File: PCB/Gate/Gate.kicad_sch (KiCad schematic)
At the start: 140 parts, among them J1 USB-C, J2 Shelly, P1 TestPoint, P10 TestPoint, P11 TestPoint, P12 TestPoint, P13 TestPoint, P2 TestPoint, P3 TestPoint, P4 TestPoint, P5 TestPoint, P6 TestPoint, P7 TestPoint, P8 TestPoint, P9 TestPoint, T1 TestPoint, T10 TestPoint, T11 TestPoint, T12 TestPoint, T13 TestPoint, T2 TestPoint, T3 TestPoint, T4 TestPoint, T5 TestPoint, T6 TestPoint, T7 TestPoint, T8 TestPoint, T9 TestPoint, U1 ESP32-PICO-MINI-02, U2 LMR16006XDDCR, U3 QR

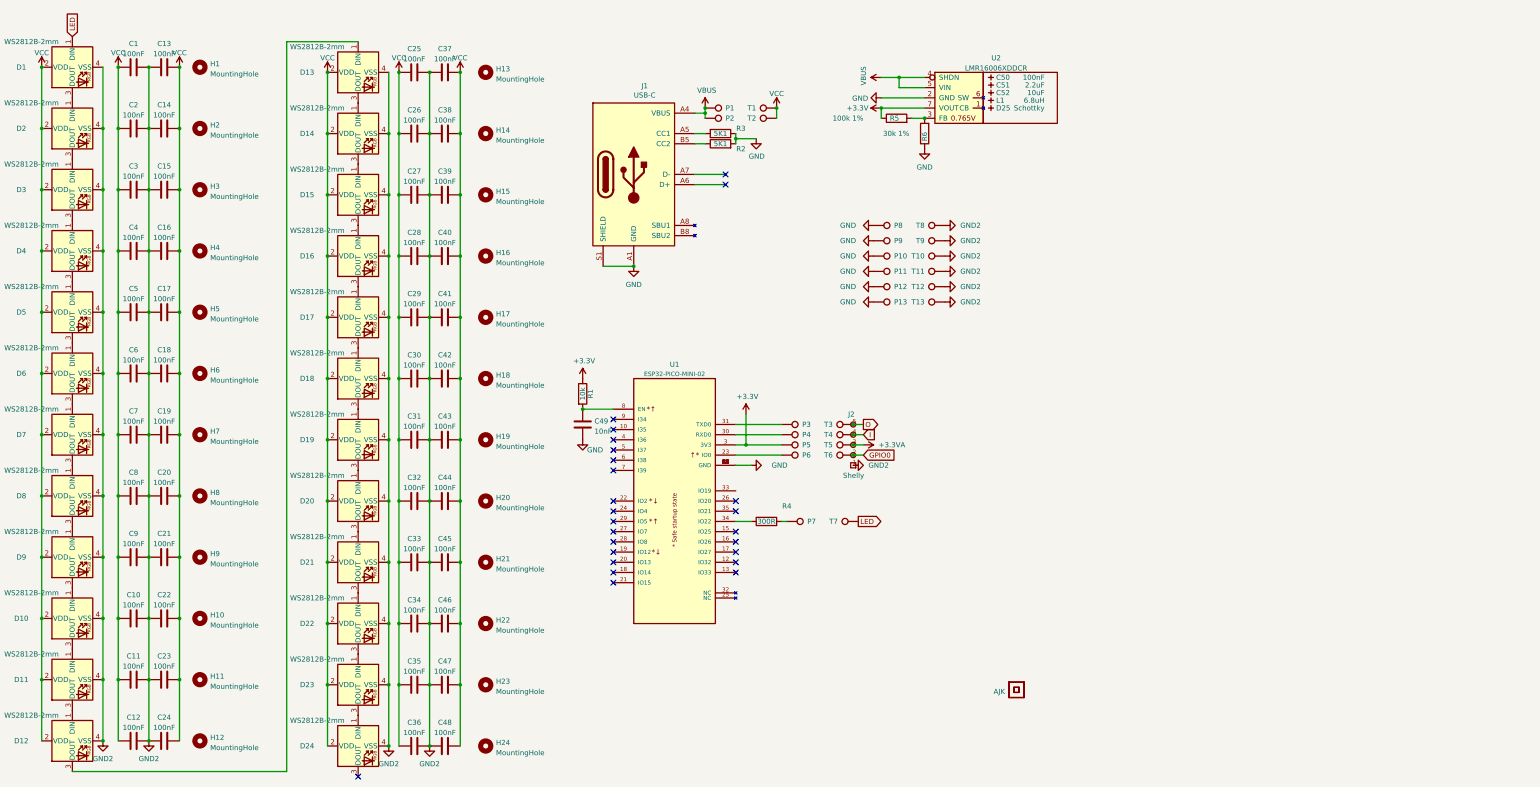
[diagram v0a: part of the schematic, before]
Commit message: Changed pads for easier soldering next time
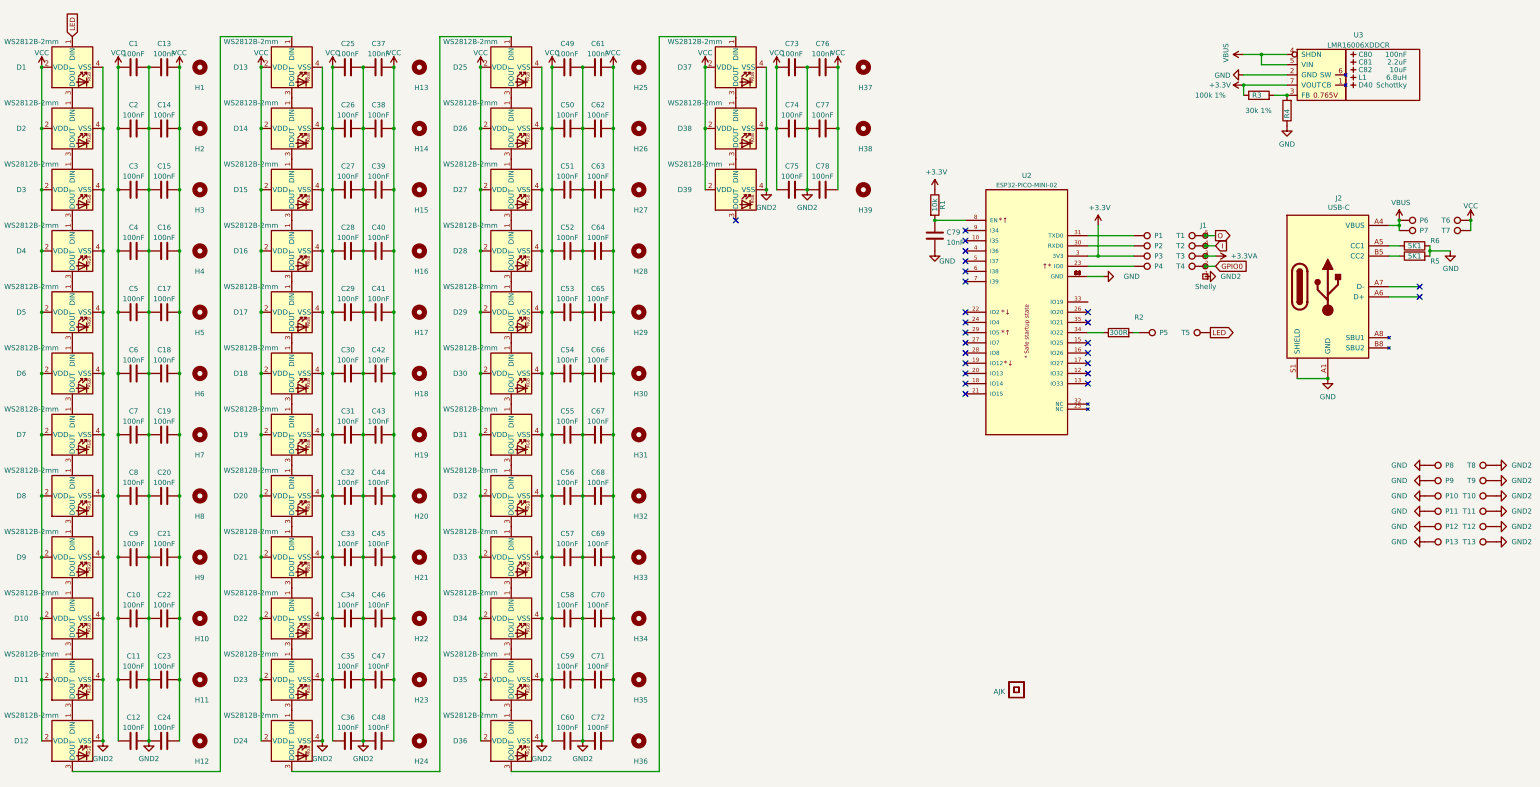
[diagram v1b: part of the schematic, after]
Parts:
- added C49, C50, C51, C52, C53, C54, C55, C56, C57, C58, C59, C60, C61, C62, C63, C64, C65, C66, C67, C68, C69, C70, C71, C72, C73, C74, C75, C76, C77, C78: 100nF, RevK:C_0603, symbol Device:C
- added D25, D26, D27, D28, D29, D30, D31, D32, D33, D34, D35, D36, D37, D38, D39: WS2812B-2mm, RevK:SMD2020, symbol RevK:WS2812B-2mm
- added H25, H26, H27, H28, H29, H30, H31, H32, H33, H34, H35, H36, H37, H38, H39: MountingHole, RevK:LEDHOLE, symbol Mechanical:MountingHole
- renumbered C49 to C79, C50 to C80, C51 to C81, C52 to C82, D25 to D40, J2 to J1, J1 to J2, P3 to P1, P4 to P2, P5 to P3, P6 to P4, P7 to P5, P1 to P6, P2 to P7, R4 to R2, R5 to R3, R6 to R4, R2 to R5, R3 to R6, T3 to T1, T4 to T2, T5 to T3, T6 to T4, T7 to T5, T1 to T6, T2 to T7, U3 to U1, U1 to U2, U2 to U3
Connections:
- net GND2: now also C49.2, C50.2, C51.2, C52.2, C53.2, C54.2, C55.2, C56.2, C57.2, C58.2, C59.2, C60.2, C61.2, C62.2, C63.2, C64.2, C65.2, C66.2, C67.2, C68.2, C69.2, C70.2, C71.2, C72.2, C73.2, C74.2, C75.2, C76.2, C77.2, C78.2, D25.4 (VSS), D26.4 (VSS), D27.4 (VSS), D28.4 (VSS), D29.4 (VSS), D30.4 (VSS), D31.4 (VSS), D32.4 (VSS), D33.4 (VSS), D34.4 (VSS), D35.4 (VSS), D36.4 (VSS), D37.4 (VSS), D38.4 (VSS), D39.4 (VSS)
- net VCC: now also C49.1, C50.1, C51.1, C52.1, C53.1, C54.1, C55.1, C56.1, C57.1, C58.1, C59.1, C60.1, C61.1, C62.1, C63.1, C64.1, C65.1, C66.1, C67.1, C68.1, C69.1, C70.1, C71.1, C72.1, C73.1, C74.1, C75.1, C76.1, C77.1, C78.1, D25.2 (VDD), D26.2 (VDD), D27.2 (VDD), D28.2 (VDD), D29.2 (VDD), D30.2 (VDD), D31.2 (VDD), D32.2 (VDD), D33.2 (VDD), D34.2 (VDD), D35.2 (VDD), D36.2 (VDD), D37.2 (VDD), D38.2 (VDD), D39.2 (VDD)
- net at D24.3 (DOUT): now also D25.1 (DIN)
- new net: D37.3 (DOUT), D38.1 (DIN)
- new net: D38.3 (DOUT), D39.1 (DIN)
- new net: D26.3 (DOUT), D27.1 (DIN)
- new net: D27.3 (DOUT), D28.1 (DIN)
- new net: D29.3 (DOUT), D30.1 (DIN)
- new net: D30.3 (DOUT), D31.1 (DIN)
- new net: D28.3 (DOUT), D29.1 (DIN)
- new net: D33.3 (DOUT), D34.1 (DIN)
- new net: D34.3 (DOUT), D35.1 (DIN)
- new net: D32.3 (DOUT), D33.1 (DIN)
- new net: D25.3 (DOUT), D26.1 (DIN)
- new net: D35.3 (DOUT), D36.1 (DIN)
- new net: D36.3 (DOUT), D37.1 (DIN)
- new net: D31.3 (DOUT), D32.1 (DIN)
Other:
- moved on the sheet: C25, C26, C27, C28, C29, C30, C31, C32, C33, C34, C35, C36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

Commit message: Start on ring
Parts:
- removed C80: 100nF, RevK:C_0603_, symbol RevK:Hidden
- removed C81: 2.2uF, RevK:C_0805_, symbol RevK:Hidden
- removed C82: 10uF, RevK:C_0805_, symbol RevK:Hidden
- removed D1, D10, D11, D12, D13, D14, D15, D16, D17, D18, D19, D2, D20, D21, D22, D23, D24, D25, D26, D27, D28, D29, D3, D30, D31, D32, D33, D34, D35, D36, D37, D38, D39, D4, D5, D6, D7, D8, D9: WS2812B-2mm, RevK:SMD2020, symbol RevK:WS2812B-2mm
- removed D40: Schottky, RevK:D_1206_, symbol RevK:Hidden
- removed H1, H10, H11, H12, H13, H14, H15, H16, H17, H18, H19, H2, H20, H21, H22, H23, H24, H25, H26, H27, H28, H29, H3, H30, H31, H32, H33, H34, H35, H36, H37, H38, H39, H4, H5, H6, H7, H8, H9: MountingHole, RevK:LEDHOLE, symbol Mechanical:MountingHole
- removed J1: Shelly, RevK:Shelly, symbol RevK:Shelly
- removed J2: USB-C, RevK:USC16-TR, symbol RevK:USB-C
- removed L1: 6.8uH, RevK:L_4x4_, symbol RevK:Hidden
- removed P1, P10, P11, P12, P13, P2, P3, P4, P5, P6, P7, P8, P9: TestPoint, RevK:PAD, symbol Connector:TestPoint
- removed R1: 10k, RevK:R_0603, symbol Device:R
- removed R2: 300R, RevK:R_0603, symbol Device:R
- removed R3: 100k 1%, RevK:R_0603, symbol Device:R
- removed R4: 30k 1%, RevK:R_0603, symbol Device:R
- removed R5, R6: 5K1, RevK:R_0603, symbol Device:R
- removed T1, T10, T11, T12, T13, T2, T3, T4, T5, T6, T7, T8, T9: TestPoint, RevK:PAD-LINK, symbol Connector:TestPoint
- removed U2: ESP32-PICO-MINI-02, RevK:ESP32-PICO-MINI-02, symbol RevK:ESP32-PICO-MINI-02
- removed U3: LMR16006XDDCR, RevK:SOT-23-Thin-6-Reg, symbol RevK:LMR16006XDDCR
- added C100, C101, C102, C103, C104, C105, C106, C107, C108, C109, C110, C111, C112, C113, C114, C115, C116, C117, C80, C81, C82, C83, C84, C85, C86, C87, C88, C89, C90, C91, C92, C93, C94, C95, C96, C97, C98, C99: 330nF, RevK:C_0402, symbol Device:C
- added D1, D10, D100, D101, D102, D103, D104, D105, D106, D107, D108, D109, D11, D110, D111, D112, D113, D114, D115, D116, D117, D12, D13, D14, D15, D16, D17, D18, D19, D2, D20, D21, D22, D23, D24, D25, D26, D27, D28, D29, D3, D30, D31, D32, D33, D34, D35, D36, D37, D38, D39, D4, D40, D41, D42, D43, D44, D45, D46, D47, D48, D49, D5, D50, D51, D52, D53, D54, D55, D56, D57, D58, D59, D6, D60, D61, D62, D63, D64, D65, D66, D67, D68, D69, D7, D70, D71, D72, D73, D74, D75, D76, D77, D78, D79, D8, D80, D81, D82, D83, D84, D85, D86, D87, D88, D89, D9, D90, D91, D92, D93, D94, D95, D96, D97, D98, D99: XL-1010RGBC-WS2812B, RevK:SMD1010, symbol RevK:WS2812B-1mm
- C1, C10, C11, C12, C13, C14, C15, C16, C17, C18, C19, C2, C20, C21, C22, C23, C24, C25, C26, C27, C28, C29, C3, C30, C31, C32, C33, C34, C35, C36, C37, C38, C39, C4, C40, C41, C42, C43, C44, C45, C46, C47, C48, C49, C5, C50, C51, C52, C53, C54, C55, C56, C57, C58, C59, C6, C60, C61, C62, C63, C64, C65, C66, C67, C68, C69, C7, C70, C71, C72, C73, C74, C75, C76, C77, C78, C8, C9: value 100nF -> 330nF; footprint RevK:C_0603 -> RevK:C_0402
- C79: value 10nF -> 330nF; footprint Capacitor_SMD:C_0603_1608Metric -> RevK:C_0402
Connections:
- net GND2 is gone; now on net GND: C1.2, C10.2, C11.2, C12.2, C13.2, C14.2, C15.2, C16.2, C17.2, C18.2, C19.2, C2.2, C20.2, C21.2, C22.2, C23.2, C24.2, C25.2, C26.2, C27.2, C28.2, C29.2, C3.2, C30.2, C31.2, C32.2, C33.2, C34.2, C35.2, C36.2, C37.2, C38.2, C39.2, C4.2, C40.2, C41.2, C42.2, C43.2, C44.2, C45.2, C46.2, C47.2, C48.2, C49.2, C5.2, C50.2, C51.2, C52.2, C53.2, C54.2, C55.2, C56.2, C57.2, C58.2, C59.2, C6.2, C60.2, C61.2, C62.2, C63.2, C64.2, C65.2, C66.2, C67.2, C68.2, C69.2, C7.2, C70.2, C71.2, C72.2, C73.2, C74.2, C75.2, C76.2, C77.2, C78.2, C8.2, C9.2
- net GND: now also C79.2, C100.2, C101.2, C102.2, C103.2, C104.2, C105.2, C106.2, C107.2, C108.2, C109.2, C110.2, C111.2, C112.2, C113.2, C114.2, C115.2, C116.2, C117.2, C80.2, C81.2, C82.2, C83.2, C84.2, C85.2, C86.2, C87.2, C88.2, C89.2, C90.2, C91.2, C92.2, C93.2, C94.2, C95.2, C96.2, C97.2, C98.2, C99.2, D1.3 (-), D10.3 (-), D100.3 (-), D101.3 (-), D102.3 (-), D103.3 (-), D104.3 (-), D105.3 (-), D106.3 (-), D107.3 (-), D108.3 (-), D109.3 (-), D11.3 (-), D110.3 (-), D111.3 (-), D112.3 (-), D113.3 (-), D114.3 (-), D115.3 (-), D116.3 (-), D117.3 (-), D12.3 (-), D13.3 (-), D14.3 (-), D15.3 (-), D16.3 (-), D17.3 (-), D18.3 (-), D19.3 (-), D2.3 (-), D20.3 (-), D21.3 (-), D22.3 (-), D23.3 (-), D24.3 (-), D25.3 (-), D26.3 (-), D27.3 (-), D28.3 (-), D29.3 (-), D3.3 (-), D30.3 (-), D31.3 (-), D32.3 (-), D33.3 (-), D34.3 (-), D35.3 (-), D36.3 (-), D37.3 (-), D38.3 (-), D39.3 (-), D4.3 (-), D40.3 (-), D41.3 (-), D42.3 (-), D43.3 (-), D44.3 (-), D45.3 (-), D46.3 (-), D47.3 (-), D48.3 (-), D49.3 (-), D5.3 (-), D50.3 (-), D51.3 (-), D52.3 (-), D53.3 (-), D54.3 (-), D55.3 (-), D56.3 (-), D57.3 (-), D58.3 (-), D59.3 (-), D6.3 (-), D60.3 (-), D61.3 (-), D62.3 (-), D63.3 (-), D64.3 (-), D65.3 (-), D66.3 (-), D67.3 (-), D68.3 (-), D69.3 (-), D7.3 (-), D70.3 (-), D71.3 (-), D72.3 (-), D73.3 (-), D74.3 (-), D75.3 (-), D76.3 (-), D77.3 (-), D78.3 (-), D79.3 (-), D8.3 (-), D80.3 (-), D81.3 (-), D82.3 (-), D83.3 (-), D84.3 (-), D85.3 (-), D86.3 (-), D87.3 (-), D88.3 (-), D89.3 (-), D9.3 (-), D90.3 (-), D91.3 (-), D92.3 (-), D93.3 (-), D94.3 (-), D95.3 (-), D96.3 (-), D97.3 (-), D98.3 (-), D99.3 (-); no longer C79.1
- net VCC: now also C79.1, C100.1, C101.1, C102.1, C103.1, C104.1, C105.1, C106.1, C107.1, C108.1, C109.1, C110.1, C111.1, C112.1, C113.1, C114.1, C115.1, C116.1, C117.1, C80.1, C81.1, C82.1, C83.1, C84.1, C85.1, C86.1, C87.1, C88.1, C89.1, C90.1, C91.1, C92.1, C93.1, C94.1, C95.1, C96.1, C97.1, C98.1, C99.1, D1.2 (+), D10.2 (+), D100.2 (+), D101.2 (+), D102.2 (+), D103.2 (+), D104.2 (+), D105.2 (+), D106.2 (+), D107.2 (+), D108.2 (+), D109.2 (+), D11.2 (+), D110.2 (+), D111.2 (+), D112.2 (+), D113.2 (+), D114.2 (+), D115.2 (+), D116.2 (+), D117.2 (+), D12.2 (+), D13.2 (+), D14.2 (+), D15.2 (+), D16.2 (+), D17.2 (+), D18.2 (+), D19.2 (+), D2.2 (+), D20.2 (+), D21.2 (+), D22.2 (+), D23.2 (+), D24.2 (+), D25.2 (+), D26.2 (+), D27.2 (+), D28.2 (+), D29.2 (+), D3.2 (+), D30.2 (+), D31.2 (+), D32.2 (+), D33.2 (+), D34.2 (+), D35.2 (+), D36.2 (+), D37.2 (+), D38.2 (+), D39.2 (+), D4.2 (+), D40.2 (+), D41.2 (+), D42.2 (+), D43.2 (+), D44.2 (+), D45.2 (+), D46.2 (+), D47.2 (+), D48.2 (+), D49.2 (+), D5.2 (+), D50.2 (+), D51.2 (+), D52.2 (+), D53.2 (+), D54.2 (+), D55.2 (+), D56.2 (+), D57.2 (+), D58.2 (+), D59.2 (+), D6.2 (+), D60.2 (+), D61.2 (+), D62.2 (+), D63.2 (+), D64.2 (+), D65.2 (+), D66.2 (+), D67.2 (+), D68.2 (+), D69.2 (+), D7.2 (+), D70.2 (+), D71.2 (+), D72.2 (+), D73.2 (+), D74.2 (+), D75.2 (+), D76.2 (+), D77.2 (+), D78.2 (+), D79.2 (+), D8.2 (+), D80.2 (+), D81.2 (+), D82.2 (+), D83.2 (+), D84.2 (+), D85.2 (+), D86.2 (+), D87.2 (+), D88.2 (+), D89.2 (+), D9.2 (+), D90.2 (+), D91.2 (+), D92.2 (+), D93.2 (+), D94.2 (+), D95.2 (+), D96.2 (+), D97.2 (+), D98.2 (+), D99.2 (+)
- new net: D109.1 (O), D110.4 (I)
- new net: D108.1 (O), D109.4 (I)
- new net: D100.1 (O), D101.4 (I)
- new net: D100.4 (I), D99.1 (O)
- new net: D83.1 (O), D84.4 (I)
- new net: D82.1 (O), D83.4 (I)
- new net: D57.1 (O), D58.4 (I)
- new net: D56.1 (O), D57.4 (I)
- new net: D77.1 (O), D78.4 (I)
- new net: D76.1 (O), D77.4 (I)
- new net: D92.1 (O), D93.4 (I)
- new net: D91.1 (O), D92.4 (I)
- new net: D32.1 (O), D33.4 (I)
- new net: D31.1 (O), D32.4 (I)
- new net: D97.1 (O), D98.4 (I)
- new net: D96.1 (O), D97.4 (I)
- new net: D20.1 (O), D21.4 (I)
- new net: D19.1 (O), D20.4 (I)
- new net: D74.1 (O), D75.4 (I)
- new net: D73.1 (O), D74.4 (I)
- new net: D45.1 (O), D46.4 (I)
- new net: D44.1 (O), D45.4 (I)
- new net: D110.1 (O), D111.4 (I)
- new net: D26.1 (O), D27.4 (I)
- new net: D25.1 (O), D26.4 (I)
- new net: D98.1 (O), D99.4 (I)
- new net: D7.1 (O), D8.4 (I)
- new net: D6.1 (O), D7.4 (I)
- new net: D55.1 (O), D56.4 (I)
- new net: D54.1 (O), D55.4 (I)
- new net: D17.1 (O), D18.4 (I)
- new net: D16.1 (O), D17.4 (I)
- new net: D24.1 (O), D25.4 (I)
- new net: D50.1 (O), D51.4 (I)
- new net: D49.1 (O), D50.4 (I)
- new net: D53.1 (O), D54.4 (I)
- new net: D52.1 (O), D53.4 (I)
- new net: D8.1 (O), D9.4 (I)
- new net: D47.1 (O), D48.4 (I)
- new net: D46.1 (O), D47.4 (I)
- new net: D43.1 (O), D44.4 (I)
- new net: D30.1 (O), D31.4 (I)
- new net: D81.1 (O), D82.4 (I)
- new net: D80.1 (O), D81.4 (I)
- new net: D35.1 (O), D36.4 (I)
- new net: D34.1 (O), D35.4 (I)
- new net: D88.1 (O), D89.4 (I)
- new net: D87.1 (O), D88.4 (I)
- new net: D90.1 (O), D91.4 (I)
- new net: D89.1 (O), D90.4 (I)
- new net: D18.1 (O), D19.4 (I)
- new net: D104.1 (O), D105.4 (I)
- new net: D103.1 (O), D104.4 (I)
- new net: D65.1 (O), D66.4 (I)
- new net: D64.1 (O), D65.4 (I)
- new net: D93.1 (O), D94.4 (I)
- new net: D29.1 (O), D30.4 (I)
- new net: D39.1 (O), D40.4 (I)
- new net: D38.1 (O), D39.4 (I)
- new net: D58.1 (O), D59.4 (I)
- new net: D67.1 (O), D68.4 (I)
- new net: D66.1 (O), D67.4 (I)
- new net: D101.1 (O), D102.4 (I)
- new net: D13.1 (O), D14.4 (I)
- new net: D12.1 (O), D13.4 (I)
- new net: D1.1 (O), D2.4 (I)
- new net: D15.1 (O), D16.4 (I)
- new net: D95.1 (O), D96.4 (I)
- new net: D94.1 (O), D95.4 (I)
- new net: D72.1 (O), D73.4 (I)
- new net: D11.1 (O), D12.4 (I)
- new net: D10.1 (O), D11.4 (I)
- new net: D116.1 (O), D117.4 (I)
- new net: D115.1 (O), D116.4 (I)
- new net: D14.1 (O), D15.4 (I)
- new net: D113.1 (O), D114.4 (I)
- new net: D112.1 (O), D113.4 (I)
- new net: D2.1 (O), D3.4 (I)
- new net: D63.1 (O), D64.4 (I)
- new net: D79.1 (O), D80.4 (I)
- new net: D78.1 (O), D79.4 (I)
- new net: D111.1 (O), D112.4 (I)
- new net: D51.1 (O), D52.4 (I)
- new net: D33.1 (O), D34.4 (I)
- new net: D28.1 (O), D29.4 (I)
- new net: D106.1 (O), D107.4 (I)
- new net: D105.1 (O), D106.4 (I)
- new net: D86.1 (O), D87.4 (I)
- new net: D71.1 (O), D72.4 (I)
- new net: D70.1 (O), D71.4 (I)
- new net: D84.1 (O), D85.4 (I)
- new net: D48.1 (O), D49.4 (I)
- new net: D22.1 (O), D23.4 (I)
- new net: D21.1 (O), D22.4 (I)
- new net: D27.1 (O), D28.4 (I)
- new net: D3.1 (O), D4.4 (I)
- new net: D85.1 (O), D86.4 (I)
- new net: D42.1 (O), D43.4 (I)
- new net: D114.1 (O), D115.4 (I)
- new net: D60.1 (O), D61.4 (I)
- new net: D59.1 (O), D60.4 (I)
- new net: D23.1 (O), D24.4 (I)
- new net: D75.1 (O), D76.4 (I)
- new net: D68.1 (O), D69.4 (I)
- new net: D10.4 (I), D9.1 (O)
- new net: D4.1 (O), D5.4 (I)
- new net: D37.1 (O), D38.4 (I)
- new net: D5.1 (O), D6.4 (I)
- new net: D62.1 (O), D63.4 (I)
- new net: D61.1 (O), D62.4 (I)
- new net: D41.1 (O), D42.4 (I)
- new net: D36.1 (O), D37.4 (I)
- new net: D102.1 (O), D103.4 (I)
- new net: D40.1 (O), D41.4 (I)
- new net: D107.1 (O), D108.4 (I)
- new net: D69.1 (O), D70.4 (I)
- no-connect marks 25 -> 0

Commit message: Gate done
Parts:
- added C118, C119, C120, C121, C122, C123, C124, C125, C126, C127, C128, C129, C130, C131, C132, C133, C134, C135, C136, C137, C138, C139, C140, C141, C142, C143, C144, C145, C146, C147, C148, C149, C150, C151, C152, C153, C154, C155, C156, C157, C158, C159, C160, C161, C162, C163, C164, C165, C166, C167, C168, C169, C170, C171, C172, C173, C174, C175, C176, C177, C178, C179, C180, C181, C182, C183, C184, C185, C186, C187, C188, C189, C190, C191, C192, C193, C194, C195, C196, C197, C198, C199, C200, C201, C202, C203, C204, C205, C206, C207, C208, C209, C210: 330nF, RevK:C_0402, symbol Device:C
- added D118, D119, D120, D121, D122, D123, D124, D125, D126, D127, D128, D129, D130, D131, D132, D133, D134, D135, D136, D137, D138, D139, D140, D141, D142, D143, D144, D145, D146, D147, D148, D149, D150, D151, D152, D153, D154, D155, D156, D157, D158, D159, D160, D161, D162, D163, D164, D165, D166, D167, D168, D169, D170, D171, D172, D173, D174, D175, D176, D177, D178, D179, D180, D181, D182, D183, D184, D185, D186, D187, D188, D189, D190, D191, D192, D193, D194, D195, D196, D197, D198, D199, D200, D201, D202, D203, D204, D205, D206, D207, D208, D209, D210: XL-1010RGBC-WS2812B, RevK:SMD1010, symbol RevK:WS2812B-1mm
- added J1, J2: Conn_01x03, RevK:3-PADS, symbol Connector_Generic:Conn_01x03
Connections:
- net GND: now also C118.2, C119.2, C120.2, C121.2, C122.2, C123.2, C124.2, C125.2, C126.2, C127.2, C128.2, C129.2, C130.2, C131.2, C132.2, C133.2, C134.2, C135.2, C136.2, C137.2, C138.2, C139.2, C140.2, C141.2, C142.2, C143.2, C144.2, C145.2, C146.2, C147.2, C148.2, C149.2, C150.2, C151.2, C152.2, C153.2, C154.2, C155.2, C156.2, C157.2, C158.2, C159.2, C160.2, C161.2, C162.2, C163.2, C164.2, C165.2, C166.2, C167.2, C168.2, C169.2, C170.2, C171.2, C172.2, C173.2, C174.2, C175.2, C176.2, C177.2, C178.2, C179.2, C180.2, C181.2, C182.2, C183.2, C184.2, C185.2, C186.2, C187.2, C188.2, C189.2, C190.2, C191.2, C192.2, C193.2, C194.2, C195.2, C196.2, C197.2, C198.2, C199.2, C200.2, C201.2, C202.2, C203.2, C204.2, C205.2, C206.2, C207.2, C208.2, C209.2, C210.2, D118.3 (-), D119.3 (-), D120.3 (-), D121.3 (-), D122.3 (-), D123.3 (-), D124.3 (-), D125.3 (-), D126.3 (-), D127.3 (-), D128.3 (-), D129.3 (-), D130.3 (-), D131.3 (-), D132.3 (-), D133.3 (-), D134.3 (-), D135.3 (-), D136.3 (-), D137.3 (-), D138.3 (-), D139.3 (-), D140.3 (-), D141.3 (-), D142.3 (-), D143.3 (-), D144.3 (-), D145.3 (-), D146.3 (-), D147.3 (-), D148.3 (-), D149.3 (-), D150.3 (-), D151.3 (-), D152.3 (-), D153.3 (-), D154.3 (-), D155.3 (-), D156.3 (-), D157.3 (-), D158.3 (-), D159.3 (-), D160.3 (-), D161.3 (-), D162.3 (-), D163.3 (-), D164.3 (-), D165.3 (-), D166.3 (-), D167.3 (-), D168.3 (-), D169.3 (-), D170.3 (-), D171.3 (-), D172.3 (-), D173.3 (-), D174.3 (-), D175.3 (-), D176.3 (-), D177.3 (-), D178.3 (-), D179.3 (-), D180.3 (-), D181.3 (-), D182.3 (-), D183.3 (-), D184.3 (-), D185.3 (-), D186.3 (-), D187.3 (-), D188.3 (-), D189.3 (-), D190.3 (-), D191.3 (-), D192.3 (-), D193.3 (-), D194.3 (-), D195.3 (-), D196.3 (-), D197.3 (-), D198.3 (-), D199.3 (-), D200.3 (-), D201.3 (-), D202.3 (-), D203.3 (-), D204.3 (-), D205.3 (-), D206.3 (-), D207.3 (-), D208.3 (-), D209.3 (-), D210.3 (-), J1.1 (Pin_1), J2.1 (Pin_1)
- net VCC: now also C118.1, C119.1, C120.1, C121.1, C122.1, C123.1, C124.1, C125.1, C126.1, C127.1, C128.1, C129.1, C130.1, C131.1, C132.1, C133.1, C134.1, C135.1, C136.1, C137.1, C138.1, C139.1, C140.1, C141.1, C142.1, C143.1, C144.1, C145.1, C146.1, C147.1, C148.1, C149.1, C150.1, C151.1, C152.1, C153.1, C154.1, C155.1, C156.1, C157.1, C158.1, C159.1, C160.1, C161.1, C162.1, C163.1, C164.1, C165.1, C166.1, C167.1, C168.1, C169.1, C170.1, C171.1, C172.1, C173.1, C174.1, C175.1, C176.1, C177.1, C178.1, C179.1, C180.1, C181.1, C182.1, C183.1, C184.1, C185.1, C186.1, C187.1, C188.1, C189.1, C190.1, C191.1, C192.1, C193.1, C194.1, C195.1, C196.1, C197.1, C198.1, C199.1, C200.1, C201.1, C202.1, C203.1, C204.1, C205.1, C206.1, C207.1, C208.1, C209.1, C210.1, D118.2 (+), D119.2 (+), D120.2 (+), D121.2 (+), D122.2 (+), D123.2 (+), D124.2 (+), D125.2 (+), D126.2 (+), D127.2 (+), D128.2 (+), D129.2 (+), D130.2 (+), D131.2 (+), D132.2 (+), D133.2 (+), D134.2 (+), D135.2 (+), D136.2 (+), D137.2 (+), D138.2 (+), D139.2 (+), D140.2 (+), D141.2 (+), D142.2 (+), D143.2 (+), D144.2 (+), D145.2 (+), D146.2 (+), D147.2 (+), D148.2 (+), D149.2 (+), D150.2 (+), D151.2 (+), D152.2 (+), D153.2 (+), D154.2 (+), D155.2 (+), D156.2 (+), D157.2 (+), D158.2 (+), D159.2 (+), D160.2 (+), D161.2 (+), D162.2 (+), D163.2 (+), D164.2 (+), D165.2 (+), D166.2 (+), D167.2 (+), D168.2 (+), D169.2 (+), D170.2 (+), D171.2 (+), D172.2 (+), D173.2 (+), D174.2 (+), D175.2 (+), D176.2 (+), D177.2 (+), D178.2 (+), D179.2 (+), D180.2 (+), D181.2 (+), D182.2 (+), D183.2 (+), D184.2 (+), D185.2 (+), D186.2 (+), D187.2 (+), D188.2 (+), D189.2 (+), D190.2 (+), D191.2 (+), D192.2 (+), D193.2 (+), D194.2 (+), D195.2 (+), D196.2 (+), D197.2 (+), D198.2 (+), D199.2 (+), D200.2 (+), D201.2 (+), D202.2 (+), D203.2 (+), D204.2 (+), D205.2 (+), D206.2 (+), D207.2 (+), D208.2 (+), D209.2 (+), D210.2 (+), J1.3 (Pin_3), J2.3 (Pin_3)
- net at D1.4 (I): now also J1.2 (Pin_2)
- net at D117.1 (O): now also D118.4 (I)
- new net: D162.1 (O), D163.4 (I)
- new net: D161.1 (O), D162.4 (I)
- new net: D187.1 (O), D188.4 (I)
- new net: D186.1 (O), D187.4 (I)
- new net: D134.1 (O), D135.4 (I)
- new net: D133.1 (O), D134.4 (I)
- new net: D182.1 (O), D183.4 (I)
- new net: D181.1 (O), D182.4 (I)
- new net: D160.1 (O), D161.4 (I)
- new net: D130.1 (O), D131.4 (I)
- new net: D129.1 (O), D130.4 (I)
- new net: D165.1 (O), D166.4 (I)
- new net: D164.1 (O), D165.4 (I)
- new net: D156.1 (O), D157.4 (I)
- new net: D155.1 (O), D156.4 (I)
- new net: D121.1 (O), D122.4 (I)
- new net: D120.1 (O), D121.4 (I)
- new net: D169.1 (O), D170.4 (I)
- new net: D168.1 (O), D169.4 (I)
- new net: D125.1 (O), D126.4 (I)
- new net: D124.1 (O), D125.4 (I)
- new net: D175.1 (O), D176.4 (I)
- new net: D174.1 (O), D175.4 (I)
- new net: D197.1 (O), D198.4 (I)
- new net: D196.1 (O), D197.4 (I)
- new net: D145.1 (O), D146.4 (I)
- new net: D144.1 (O), D145.4 (I)
- new net: D179.1 (O), D180.4 (I)
- new net: D178.1 (O), D179.4 (I)
- new net: D119.1 (O), D120.4 (I)
- new net: D202.1 (O), D203.4 (I)
- new net: D201.1 (O), D202.4 (I)
- new net: D140.1 (O), D141.4 (I)
- new net: D139.1 (O), D140.4 (I)
- new net: D191.1 (O), D192.4 (I)
- new net: D190.1 (O), D191.4 (I)
- new net: D199.1 (O), D200.4 (I)
- new net: D198.1 (O), D199.4 (I)
- new net: D184.1 (O), D185.4 (I)
- new net: D183.1 (O), D184.4 (I)
- new net: D154.1 (O), D155.4 (I)
- new net: D153.1 (O), D154.4 (I)
- new net: D138.1 (O), D139.4 (I)
- new net: D137.1 (O), D138.4 (I)
- new net: D210.1 (O), J2.2 (Pin_2)
- new net: D173.1 (O), D174.4 (I)
- new net: D123.1 (O), D124.4 (I)
- new net: D122.1 (O), D123.4 (I)
- new net: D148.1 (O), D149.4 (I)
- new net: D147.1 (O), D148.4 (I)
- new net: D158.1 (O), D159.4 (I)
- new net: D157.1 (O), D158.4 (I)
- new net: D152.1 (O), D153.4 (I)
- new net: D151.1 (O), D152.4 (I)
- new net: D185.1 (O), D186.4 (I)
- new net: D206.1 (O), D207.4 (I)
- new net: D205.1 (O), D206.4 (I)
- new net: D150.1 (O), D151.4 (I)
- new net: D170.1 (O), D171.4 (I)
- new net: D177.1 (O), D178.4 (I)
- new net: D176.1 (O), D177.4 (I)
- new net: D203.1 (O), D204.4 (I)
- new net: D146.1 (O), D147.4 (I)
- new net: D131.1 (O), D132.4 (I)
- new net: D118.1 (O), D119.4 (I)
- new net: D126.1 (O), D127.4 (I)
- new net: D132.1 (O), D133.4 (I)
- new net: D180.1 (O), D181.4 (I)
- new net: D172.1 (O), D173.4 (I)
- new net: D167.1 (O), D168.4 (I)
- new net: D143.1 (O), D144.4 (I)
- new net: D142.1 (O), D143.4 (I)
- new net: D136.1 (O), D137.4 (I)
- new net: D135.1 (O), D136.4 (I)
- new net: D149.1 (O), D150.4 (I)
- new net: D188.1 (O), D189.4 (I)
- new net: D200.1 (O), D201.4 (I)
- new net: D194.1 (O), D195.4 (I)
- new net: D193.1 (O), D194.4 (I)
- new net: D189.1 (O), D190.4 (I)
- new net: D204.1 (O), D205.4 (I)
- new net: D141.1 (O), D142.4 (I)
- new net: D163.1 (O), D164.4 (I)
- new net: D166.1 (O), D167.4 (I)
- new net: D171.1 (O), D172.4 (I)
- new net: D195.1 (O), D196.4 (I)
- new net: D128.1 (O), D129.4 (I)
- new net: D127.1 (O), D128.4 (I)
- new net: D207.1 (O), D208.4 (I)
- new net: D192.1 (O), D193.4 (I)
- new net: D209.1 (O), D210.4 (I)
- new net: D208.1 (O), D209.4 (I)
- new net: D159.1 (O), D160.4 (I)
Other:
- moved on the sheet: C1, C10, C100, C101, C102, C103, C104, C105, C106, C107, C108, C109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

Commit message: Redone
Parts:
- removed Logo1: AJK, RevK:AJK, symbol RevK:AJK
- removed U1: QR, RevK:QR-LED, symbol RevK:QR
- added C211, C212, C213, C214, C215, C216, C217, C218, C219, C220, C221, C222, C223, C224, C225, C226, C227, C228, C229, C230, C231, C232, C233, C234, C235, C236, C237, C238, C239, C240, C241, C242, C243, C244, C245, C246, C247, C248, C249, C250, C251, C252, C253, C254, C255, C256, C257, C258, C259, C260, C261, C262, C263, C264, C265, C266, C267, C268, C269, C270, C271, C272, C273, C274, C275, C276, C277, C278, C279, C280, C281, C282, C283, C284, C285, C286, C287, C288, C289, C290, C291, C292, C293, C294, C295, C296, C297, C298, C299, C300, C301, C302, C303, C304, C305, C306, C307, C308, C309, C310, C311, C312, C313, C314, C315, C316, C317, C318, C319, C320, C321, C322, C323, C324, C325, C326, C327, C328, C329, C330, C331, C332, C333, C334, C335, C336, C337, C338, C339, C340, C341, C342, C343, C344, C345, C346, C347, C348, C349, C350, C351, C352, C353, C354, C355, C356, C357, C358, C359, C360, C361, C362, C363, C364, C365, C366, C367, C368, C369, C370, C371, C372: 330nF, RevK:C_0402, symbol Device:C
- added D211, D212, D213, D214, D215, D216, D217, D218, D219, D220, D221, D222, D223, D224, D225, D226, D227, D228, D229, D230, D231, D232, D233, D234, D235, D236, D237, D238, D239, D240, D241, D242, D243, D244, D245, D246, D247, D248, D249, D250, D251, D252, D253, D254, D255, D256, D257, D258, D259, D260, D261, D262, D263, D264, D265, D266, D267, D268, D269, D270, D271, D272, D273, D274, D275, D276, D277, D278, D279, D280, D281, D282, D283, D284, D285, D286, D287, D288, D289, D290, D291, D292, D293, D294, D295, D296, D297, D298, D299, D300, D301, D302, D303, D304, D305, D306, D307, D308, D309, D310, D311, D312, D313, D314, D315, D316, D317, D318, D319, D320, D321, D322, D323, D324, D325, D326, D327, D328, D329, D330, D331, D332, D333, D334, D335, D336, D337, D338, D339, D340, D341, D342, D343, D344, D345, D346, D347, D348, D349, D350, D351, D352, D353, D354, D355, D356, D357, D358, D359, D360, D361, D362, D363, D364, D365, D366, D367, D368, D369, D370, D371, D372: XL-1010RGBC-WS2812B, RevK:SMD1010, symbol RevK:WS2812B-1mm
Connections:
- net GND: now also C211.2, C212.2, C213.2, C214.2, C215.2, C216.2, C217.2, C218.2, C219.2, C220.2, C221.2, C222.2, C223.2, C224.2, C225.2, C226.2, C227.2, C228.2, C229.2, C230.2, C231.2, C232.2, C233.2, C234.2, C235.2, C236.2, C237.2, C238.2, C239.2, C240.2, C241.2, C242.2, C243.2, C244.2, C245.2, C246.2, C247.2, C248.2, C249.2, C250.2, C251.2, C252.2, C253.2, C254.2, C255.2, C256.2, C257.2, C258.2, C259.2, C260.2, C261.2, C262.2, C263.2, C264.2, C265.2, C266.2, C267.2, C268.2, C269.2, C270.2, C271.2, C272.2, C273.2, C274.2, C275.2, C276.2, C277.2, C278.2, C279.2, C280.2, C281.2, C282.2, C283.2, C284.2, C285.2, C286.2, C287.2, C288.2, C289.2, C290.2, C291.2, C292.2, C293.2, C294.2, C295.2, C296.2, C297.2, C298.2, C299.2, C300.2, C301.2, C302.2, C303.2, C304.2, C305.2, C306.2, C307.2, C308.2, C309.2, C310.2, C311.2, C312.2, C313.2, C314.2, C315.2, C316.2, C317.2, C318.2, C319.2, C320.2, C321.2, C322.2, C323.2, C324.2, C325.2, C326.2, C327.2, C328.2, C329.2, C330.2, C331.2, C332.2, C333.2, C334.2, C335.2, C336.2, C337.2, C338.2, C339.2, C340.2, C341.2, C342.2, C343.2, C344.2, C345.2, C346.2, C347.2, C348.2, C349.2, C350.2, C351.2, C352.2, C353.2, C354.2, C355.2, C356.2, C357.2, C358.2, C359.2, C360.2, C361.2, C362.2, C363.2, C364.2, C365.2, C366.2, C367.2, C368.2, C369.2, C370.2, C371.2, C372.2, D211.3 (-), D212.3 (-), D213.3 (-), D214.3 (-), D215.3 (-), D216.3 (-), D217.3 (-), D218.3 (-), D219.3 (-), D220.3 (-), D221.3 (-), D222.3 (-), D223.3 (-), D224.3 (-), D225.3 (-), D226.3 (-), D227.3 (-), D228.3 (-), D229.3 (-), D230.3 (-), D231.3 (-), D232.3 (-), D233.3 (-), D234.3 (-), D235.3 (-), D236.3 (-), D237.3 (-), D238.3 (-), D239.3 (-), D240.3 (-), D241.3 (-), D242.3 (-), D243.3 (-), D244.3 (-), D245.3 (-), D246.3 (-), D247.3 (-), D248.3 (-), D249.3 (-), D250.3 (-), D251.3 (-), D252.3 (-), D253.3 (-), D254.3 (-), D255.3 (-), D256.3 (-), D257.3 (-), D258.3 (-), D259.3 (-), D260.3 (-), D261.3 (-), D262.3 (-), D263.3 (-), D264.3 (-), D265.3 (-), D266.3 (-), D267.3 (-), D268.3 (-), D269.3 (-), D270.3 (-), D271.3 (-), D272.3 (-), D273.3 (-), D274.3 (-), D275.3 (-), D276.3 (-), D277.3 (-), D278.3 (-), D279.3 (-), D280.3 (-), D281.3 (-), D282.3 (-), D283.3 (-), D284.3 (-), D285.3 (-), D286.3 (-), D287.3 (-), D288.3 (-), D289.3 (-), D290.3 (-), D291.3 (-), D292.3 (-), D293.3 (-), D294.3 (-), D295.3 (-), D296.3 (-), D297.3 (-), D298.3 (-), D299.3 (-), D300.3 (-), D301.3 (-), D302.3 (-), D303.3 (-), D304.3 (-), D305.3 (-), D306.3 (-), D307.3 (-), D308.3 (-), D309.3 (-), D310.3 (-), D311.3 (-), D312.3 (-), D313.3 (-), D314.3 (-), D315.3 (-), D316.3 (-), D317.3 (-), D318.3 (-), D319.3 (-), D320.3 (-), D321.3 (-), D322.3 (-), D323.3 (-), D324.3 (-), D325.3 (-), D326.3 (-), D327.3 (-), D328.3 (-), D329.3 (-), D330.3 (-), D331.3 (-), D332.3 (-), D333.3 (-), D334.3 (-), D335.3 (-), D336.3 (-), D337.3 (-), D338.3 (-), D339.3 (-), D340.3 (-), D341.3 (-), D342.3 (-), D343.3 (-), D344.3 (-), D345.3 (-), D346.3 (-), D347.3 (-), D348.3 (-), D349.3 (-), D350.3 (-), D351.3 (-), D352.3 (-), D353.3 (-), D354.3 (-), D355.3 (-), D356.3 (-), D357.3 (-), D358.3 (-), D359.3 (-), D360.3 (-), D361.3 (-), D362.3 (-), D363.3 (-), D364.3 (-), D365.3 (-), D366.3 (-), D367.3 (-), D368.3 (-), D369.3 (-), D370.3 (-), D371.3 (-), D372.3 (-)
- net VCC: now also C211.1, C212.1, C213.1, C214.1, C215.1, C216.1, C217.1, C218.1, C219.1, C220.1, C221.1, C222.1, C223.1, C224.1, C225.1, C226.1, C227.1, C228.1, C229.1, C230.1, C231.1, C232.1, C233.1, C234.1, C235.1, C236.1, C237.1, C238.1, C239.1, C240.1, C241.1, C242.1, C243.1, C244.1, C245.1, C246.1, C247.1, C248.1, C249.1, C250.1, C251.1, C252.1, C253.1, C254.1, C255.1, C256.1, C257.1, C258.1, C259.1, C260.1, C261.1, C262.1, C263.1, C264.1, C265.1, C266.1, C267.1, C268.1, C269.1, C270.1, C271.1, C272.1, C273.1, C274.1, C275.1, C276.1, C277.1, C278.1, C279.1, C280.1, C281.1, C282.1, C283.1, C284.1, C285.1, C286.1, C287.1, C288.1, C289.1, C290.1, C291.1, C292.1, C293.1, C294.1, C295.1, C296.1, C297.1, C298.1, C299.1, C300.1, C301.1, C302.1, C303.1, C304.1, C305.1, C306.1, C307.1, C308.1, C309.1, C310.1, C311.1, C312.1, C313.1, C314.1, C315.1, C316.1, C317.1, C318.1, C319.1, C320.1, C321.1, C322.1, C323.1, C324.1, C325.1, C326.1, C327.1, C328.1, C329.1, C330.1, C331.1, C332.1, C333.1, C334.1, C335.1, C336.1, C337.1, C338.1, C339.1, C340.1, C341.1, C342.1, C343.1, C344.1, C345.1, C346.1, C347.1, C348.1, C349.1, C350.1, C351.1, C352.1, C353.1, C354.1, C355.1, C356.1, C357.1, C358.1, C359.1, C360.1, C361.1, C362.1, C363.1, C364.1, C365.1, C366.1, C367.1, C368.1, C369.1, C370.1, C371.1, C372.1, D211.2 (+), D212.2 (+), D213.2 (+), D214.2 (+), D215.2 (+), D216.2 (+), D217.2 (+), D218.2 (+), D219.2 (+), D220.2 (+), D221.2 (+), D222.2 (+), D223.2 (+), D224.2 (+), D225.2 (+), D226.2 (+), D227.2 (+), D228.2 (+), D229.2 (+), D230.2 (+), D231.2 (+), D232.2 (+), D233.2 (+), D234.2 (+), D235.2 (+), D236.2 (+), D237.2 (+), D238.2 (+), D239.2 (+), D240.2 (+), D241.2 (+), D242.2 (+), D243.2 (+), D244.2 (+), D245.2 (+), D246.2 (+), D247.2 (+), D248.2 (+), D249.2 (+), D250.2 (+), D251.2 (+), D252.2 (+), D253.2 (+), D254.2 (+), D255.2 (+), D256.2 (+), D257.2 (+), D258.2 (+), D259.2 (+), D260.2 (+), D261.2 (+), D262.2 (+), D263.2 (+), D264.2 (+), D265.2 (+), D266.2 (+), D267.2 (+), D268.2 (+), D269.2 (+), D270.2 (+), D271.2 (+), D272.2 (+), D273.2 (+), D274.2 (+), D275.2 (+), D276.2 (+), D277.2 (+), D278.2 (+), D279.2 (+), D280.2 (+), D281.2 (+), D282.2 (+), D283.2 (+), D284.2 (+), D285.2 (+), D286.2 (+), D287.2 (+), D288.2 (+), D289.2 (+), D290.2 (+), D291.2 (+), D292.2 (+), D293.2 (+), D294.2 (+), D295.2 (+), D296.2 (+), D297.2 (+), D298.2 (+), D299.2 (+), D300.2 (+), D301.2 (+), D302.2 (+), D303.2 (+), D304.2 (+), D305.2 (+), D306.2 (+), D307.2 (+), D308.2 (+), D309.2 (+), D310.2 (+), D311.2 (+), D312.2 (+), D313.2 (+), D314.2 (+), D315.2 (+), D316.2 (+), D317.2 (+), D318.2 (+), D319.2 (+), D320.2 (+), D321.2 (+), D322.2 (+), D323.2 (+), D324.2 (+), D325.2 (+), D326.2 (+), D327.2 (+), D328.2 (+), D329.2 (+), D330.2 (+), D331.2 (+), D332.2 (+), D333.2 (+), D334.2 (+), D335.2 (+), D336.2 (+), D337.2 (+), D338.2 (+), D339.2 (+), D340.2 (+), D341.2 (+), D342.2 (+), D343.2 (+), D344.2 (+), D345.2 (+), D346.2 (+), D347.2 (+), D348.2 (+), D349.2 (+), D350.2 (+), D351.2 (+), D352.2 (+), D353.2 (+), D354.2 (+), D355.2 (+), D356.2 (+), D357.2 (+), D358.2 (+), D359.2 (+), D360.2 (+), D361.2 (+), D362.2 (+), D363.2 (+), D364.2 (+), D365.2 (+), D366.2 (+), D367.2 (+), D368.2 (+), D369.2 (+), D370.2 (+), D371.2 (+), D372.2 (+)
- net at D210.1 (O): now also D211.4 (I); no longer J2.2 (Pin_2)
- new net: D263.1 (O), D264.4 (I)
- new net: D262.1 (O), D263.4 (I)
- new net: D287.1 (O), D288.4 (I)
- new net: D286.1 (O), D287.4 (I)
- new net: D364.1 (O), D365.4 (I)
- new net: D363.1 (O), D364.4 (I)
- new net: D308.1 (O), D309.4 (I)
- new net: D307.1 (O), D308.4 (I)
- new net: D347.1 (O), D348.4 (I)
- new net: D346.1 (O), D347.4 (I)
- new net: D326.1 (O), D327.4 (I)
- new net: D325.1 (O), D326.4 (I)
- new net: D305.1 (O), D306.4 (I)
- new net: D304.1 (O), D305.4 (I)
- new net: D352.1 (O), D353.4 (I)
- new net: D351.1 (O), D352.4 (I)
- new net: D324.1 (O), D325.4 (I)
- new net: D294.1 (O), D295.4 (I)
- new net: D293.1 (O), D294.4 (I)
- new net: D296.1 (O), D297.4 (I)
- new net: D295.1 (O), D296.4 (I)
- new net: D271.1 (O), D272.4 (I)
- new net: D270.1 (O), D271.4 (I)
- new net: D244.1 (O), D245.4 (I)
- new net: D243.1 (O), D244.4 (I)
- new net: D261.1 (O), D262.4 (I)
- new net: D246.1 (O), D247.4 (I)
- new net: D245.1 (O), D246.4 (I)
- new net: D371.1 (O), D372.4 (I)
- new net: D370.1 (O), D371.4 (I)
- new net: D257.1 (O), D258.4 (I)
- new net: D256.1 (O), D257.4 (I)
- new net: D330.1 (O), D331.4 (I)
- new net: D329.1 (O), D330.4 (I)
- new net: D231.1 (O), D232.4 (I)
- new net: D230.1 (O), D231.4 (I)
- new net: D312.1 (O), D313.4 (I)
- new net: D311.1 (O), D312.4 (I)
- new net: D247.1 (O), D248.4 (I)
- new net: D260.1 (O), D261.4 (I)
- new net: D240.1 (O), D241.4 (I)
- new net: D239.1 (O), D240.4 (I)
- new net: D282.1 (O), D283.4 (I)
- new net: D281.1 (O), D282.4 (I)
- new net: D328.1 (O), D329.4 (I)
- new net: D253.1 (O), D254.4 (I)
- new net: D252.1 (O), D253.4 (I)
- new net: D251.1 (O), D252.4 (I)
- new net: D249.1 (O), D250.4 (I)
- new net: D248.1 (O), D249.4 (I)
- new net: D269.1 (O), D270.4 (I)
- new net: D280.1 (O), D281.4 (I)
- new net: D279.1 (O), D280.4 (I)
- new net: D290.1 (O), D291.4 (I)
- new net: D289.1 (O), D290.4 (I)
- new net: D356.1 (O), D357.4 (I)
- new net: D355.1 (O), D356.4 (I)
- new net: D342.1 (O), D343.4 (I)
- new net: D341.1 (O), D342.4 (I)
- new net: D278.1 (O), D279.4 (I)
- new net: D277.1 (O), D278.4 (I)
- new net: D338.1 (O), D339.4 (I)
- new net: D337.1 (O), D338.4 (I)
- new net: D228.1 (O), D229.4 (I)
- new net: D227.1 (O), D228.4 (I)
- new net: D259.1 (O), D260.4 (I)
- new net: D331.1 (O), D332.4 (I)
- new net: D224.1 (O), D225.4 (I)
- new net: D223.1 (O), D224.4 (I)
- new net: D310.1 (O), D311.4 (I)
- new net: D300.1 (O), D301.4 (I)
- new net: D299.1 (O), D300.4 (I)
- new net: D242.1 (O), D243.4 (I)
- new net: D241.1 (O), D242.4 (I)
- new net: D211.1 (O), D212.4 (I)
- new net: D336.1 (O), D337.4 (I)
- new net: D335.1 (O), D336.4 (I)
- new net: D372.1 (O), J2.2 (Pin_2)
- new net: D250.1 (O), D251.4 (I)
- new net: D362.1 (O), D363.4 (I)
- new net: D327.1 (O), D328.4 (I)
- new net: D229.1 (O), D230.4 (I)
- new net: D258.1 (O), D259.4 (I)
- new net: D369.1 (O), D370.4 (I)
- new net: D368.1 (O), D369.4 (I)
- new net: D268.1 (O), D269.4 (I)
- new net: D267.1 (O), D268.4 (I)
- new net: D234.1 (O), D235.4 (I)
- new net: D233.1 (O), D234.4 (I)
- new net: D212.1 (O), D213.4 (I)
- new net: D285.1 (O), D286.4 (I)
- new net: D284.1 (O), D285.4 (I)
- new net: D343.1 (O), D344.4 (I)
- new net: D288.1 (O), D289.4 (I)
- new net: D349.1 (O), D350.4 (I)
- new net: D348.1 (O), D349.4 (I)
- new net: D320.1 (O), D321.4 (I)
- new net: D319.1 (O), D320.4 (I)
- new net: D350.1 (O), D351.4 (I)
- new net: D353.1 (O), D354.4 (I)
- new net: D354.1 (O), D355.4 (I)
- new net: D298.1 (O), D299.4 (I)
- new net: D297.1 (O), D298.4 (I)
- new net: D323.1 (O), D324.4 (I)
- new net: D322.1 (O), D323.4 (I)
- new net: D345.1 (O), D346.4 (I)
- new net: D344.1 (O), D345.4 (I)
- new net: D266.1 (O), D267.4 (I)
- new net: D265.1 (O), D266.4 (I)
- new net: D216.1 (O), D217.4 (I)
- new net: D215.1 (O), D216.4 (I)
- new net: D360.1 (O), D361.4 (I)
- new net: D359.1 (O), D360.4 (I)
- new net: D291.1 (O), D292.4 (I)
- new net: D361.1 (O), D362.4 (I)
- new net: D232.1 (O), D233.4 (I)
- new net: D222.1 (O), D223.4 (I)
- new net: D221.1 (O), D222.4 (I)
- new net: D321.1 (O), D322.4 (I)
- new net: D217.1 (O), D218.4 (I)
- new net: D255.1 (O), D256.4 (I)
- new net: D226.1 (O), D227.4 (I)
- new net: D225.1 (O), D226.4 (I)
- new net: D301.1 (O), D302.4 (I)
- new net: D264.1 (O), D265.4 (I)
- new net: D275.1 (O), D276.4 (I)
- new net: D274.1 (O), D275.4 (I)
- new net: D276.1 (O), D277.4 (I)
- new net: D306.1 (O), D307.4 (I)
- new net: D332.1 (O), D333.4 (I)
- new net: D238.1 (O), D239.4 (I)
- new net: D237.1 (O), D238.4 (I)
- new net: D314.1 (O), D315.4 (I)
- new net: D313.1 (O), D314.4 (I)
- new net: D339.1 (O), D340.4 (I)
- new net: D254.1 (O), D255.4 (I)
- new net: D333.1 (O), D334.4 (I)
- new net: D309.1 (O), D310.4 (I)
- new net: D340.1 (O), D341.4 (I)
- new net: D317.1 (O), D318.4 (I)
- new net: D316.1 (O), D317.4 (I)
- new net: D365.1 (O), D366.4 (I)
- new net: D273.1 (O), D274.4 (I)
- new net: D272.1 (O), D273.4 (I)
- new net: D358.1 (O), D359.4 (I)
- new net: D357.1 (O), D358.4 (I)
- new net: D236.1 (O), D237.4 (I)
- new net: D235.1 (O), D236.4 (I)
- new net: D214.1 (O), D215.4 (I)
- new net: D218.1 (O), D219.4 (I)
- new net: D315.1 (O), D316.4 (I)
- new net: D292.1 (O), D293.4 (I)
- new net: D213.1 (O), D214.4 (I)
- new net: D334.1 (O), D335.4 (I)
- new net: D367.1 (O), D368.4 (I)
- new net: D302.1 (O), D303.4 (I)
- new net: D283.1 (O), D284.4 (I)
- new net: D303.1 (O), D304.4 (I)
- new net: D219.1 (O), D220.4 (I)
- new net: D366.1 (O), D367.4 (I)
- new net: D220.1 (O), D221.4 (I)
- new net: D318.1 (O), D319.4 (I)
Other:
- moved on the sheet: J2
